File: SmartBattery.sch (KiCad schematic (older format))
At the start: 25 parts, among them J13 Conn_01x03_Male, J14 Conn_01x03_Male, Q22 AO3401A, U14 HT7533-1

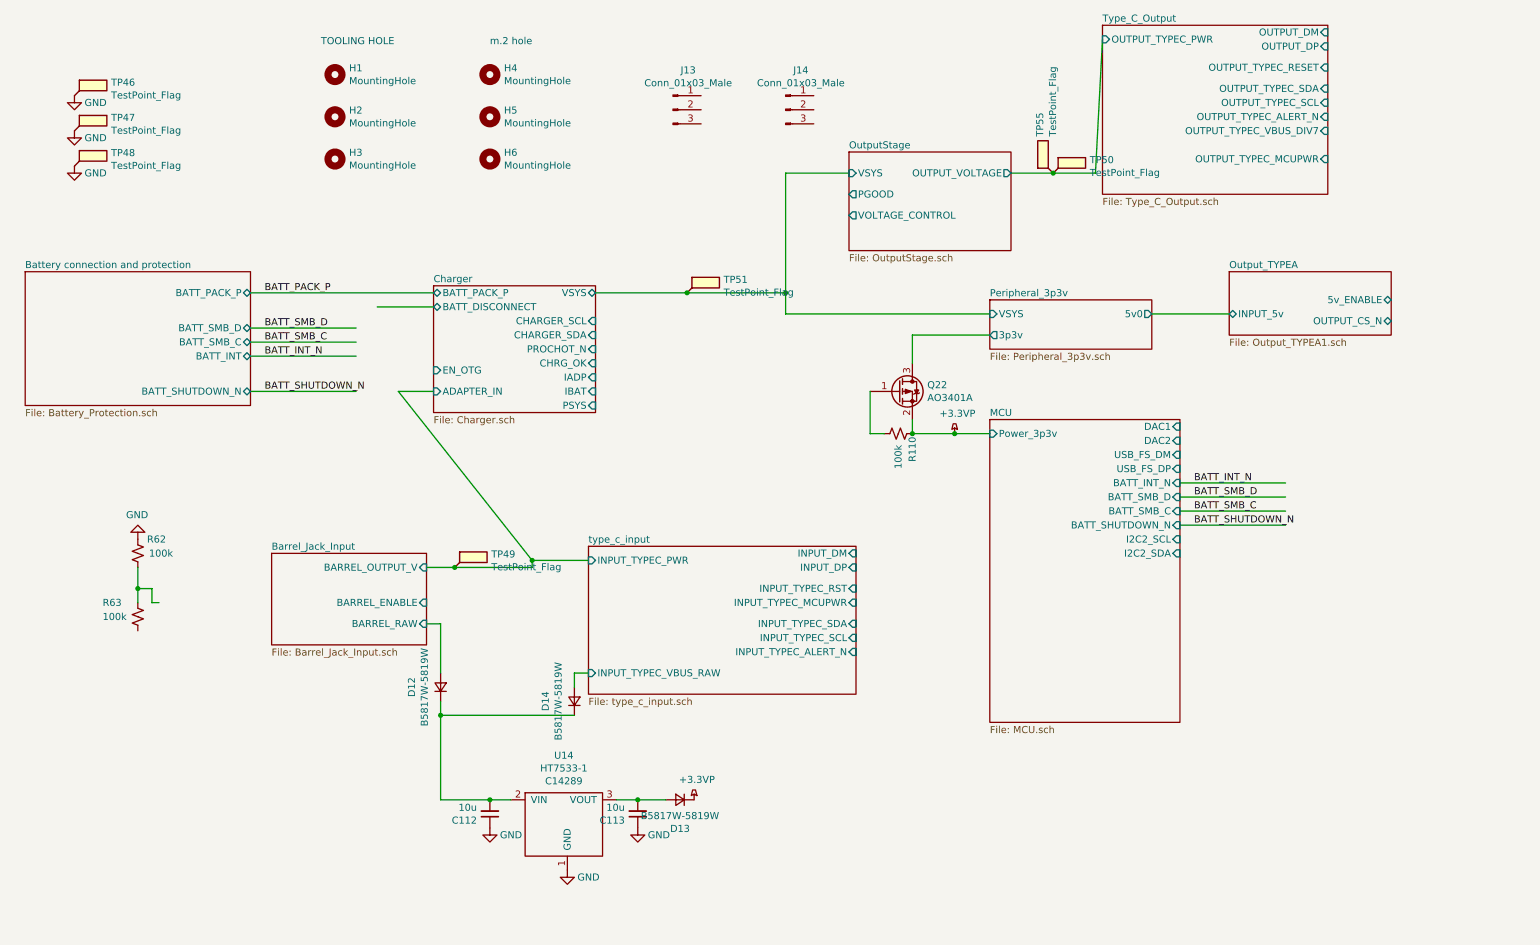
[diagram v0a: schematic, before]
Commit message: lots of GPIO connectivity changes. fixed no PD on input fixed CH340G leakage. can otherwise power from GPIO. added fet for powering VCONN from 3v/5v NEED TO ADD OVERCURRENT
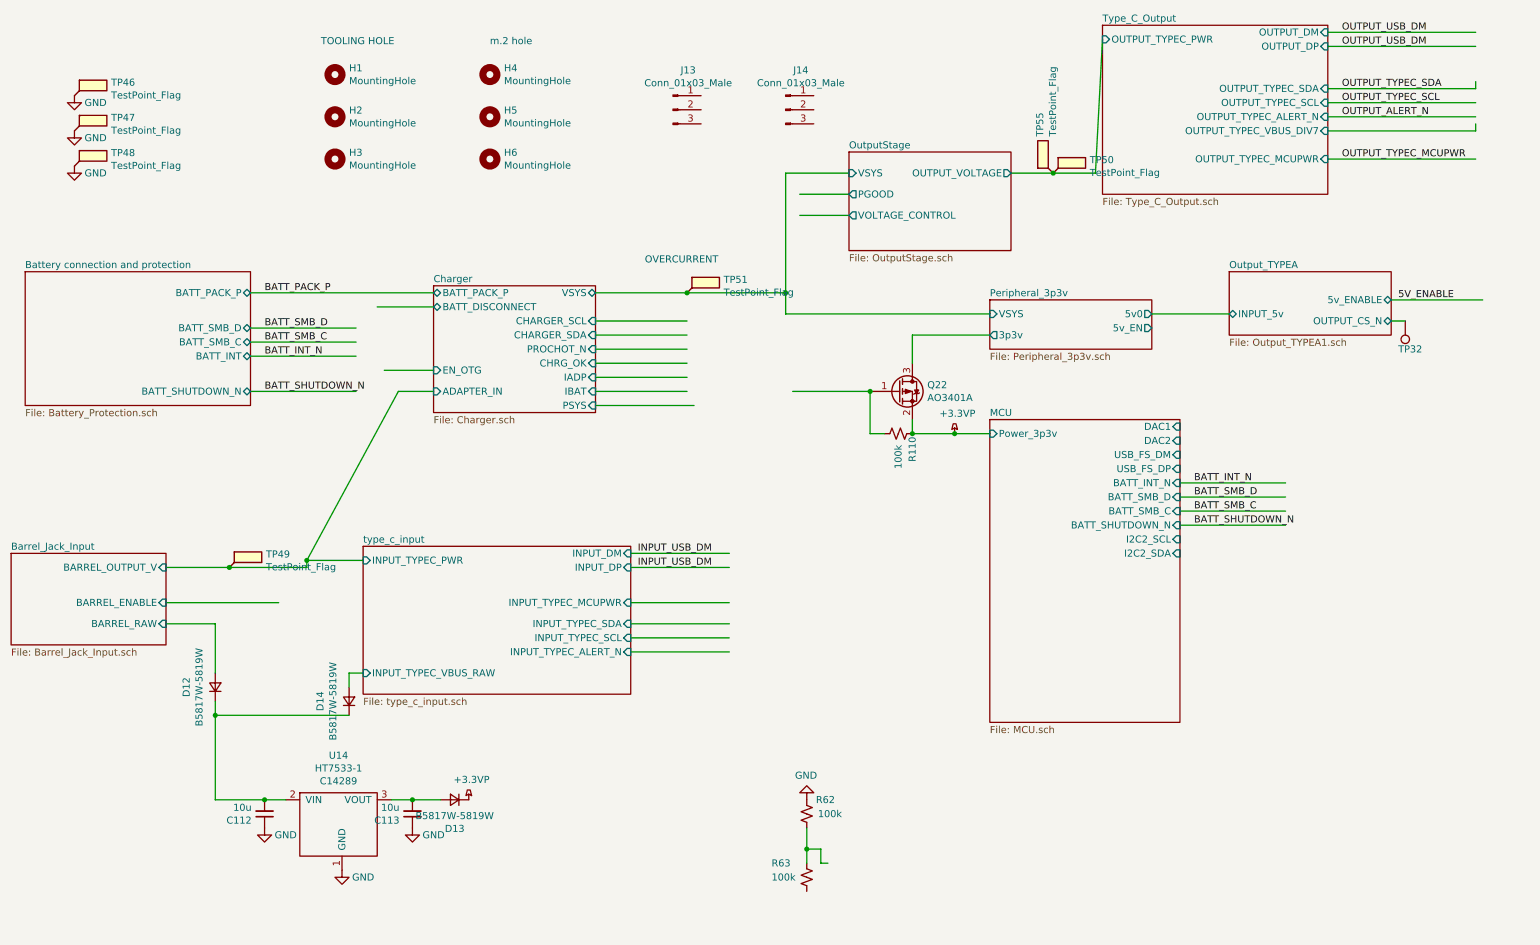
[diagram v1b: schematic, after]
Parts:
- added TP32: TestPoint, TestPoint:TestPoint_Pad_D2.0mm, symbol Connector:TestPoint
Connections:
- net labels added: 5V_ENABLE, INPUT_USB_DM, OUTPUT_ALERT_N, OUTPUT_TYPEC_MCUPWR, OUTPUT_TYPEC_SCL, OUTPUT_TYPEC_SDA, OUTPUT_USB_DM
- wire segments 49 -> 78
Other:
- note added: "OVERCURRENT"
- moved on the sheet: C112, C113, D12, D13, D14, R62, R63, TP49, U14

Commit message: Modified connections, added current limit
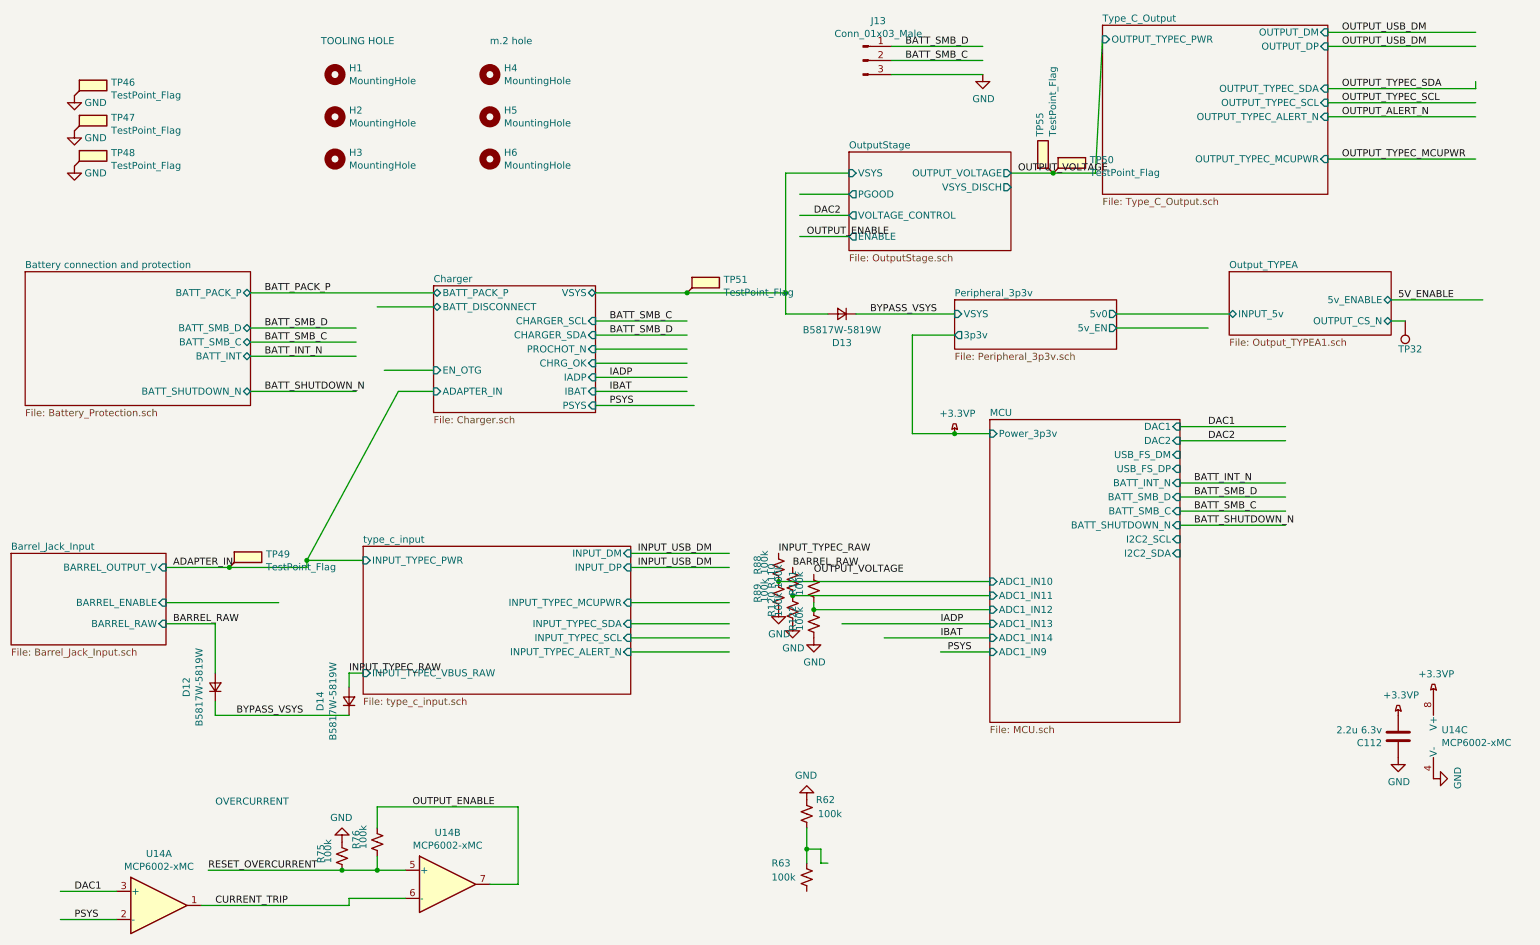
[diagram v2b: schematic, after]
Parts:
- removed C112, C113: 10u, lc_lib:0805_C, symbol Device:C_Small
- removed J14: Conn_01x03_Male, Connector_PinHeader_2.54mm:PinHeader_1x03_P2.54mm_Vertical, symbol Connector:Conn_01x03_Male
- removed Q22: AO3401A, lc_lib:SOT-23(SOT-23-3), symbol Device:Q_PMOS_GSD
- removed U14: HT7533-1, lc_lib:SOT-89(SOT-89-3), symbol SmartBattery:HT7533-1
- added C112: 2.2u 6.3v, lc_lib:0805_C, symbol Device:C
- added R120, R121, R122, R75, R76, R88, R89: 100k, lc_lib:0402_R, symbol Device:R_Small_US
- added U14: MCP6002-xMC, lc_lib:SOIC-8_150MIL, symbol Amplifier_Operational:MCP6002-xMC
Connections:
- net labels added: ADAPTER_IN, BARREL_RAW, BYPASS_VSYS, CURRENT_TRIP, DAC1, DAC2, IADP, IBAT, INPUT_TYPEC_RAW, OUTPUT_ENABLE, OUTPUT_VOLTAGE, PSYS, RESET_OVERCURRENT
- wire segments 78 -> 95
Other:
- moved on the sheet: D13, J13
